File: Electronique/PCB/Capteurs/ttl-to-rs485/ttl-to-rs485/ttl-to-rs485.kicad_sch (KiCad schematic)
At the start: 4 parts, among them U1 HW-221, U2 JST-SH 4, U3 JST-SH4 motor, U4 TTL-RS485

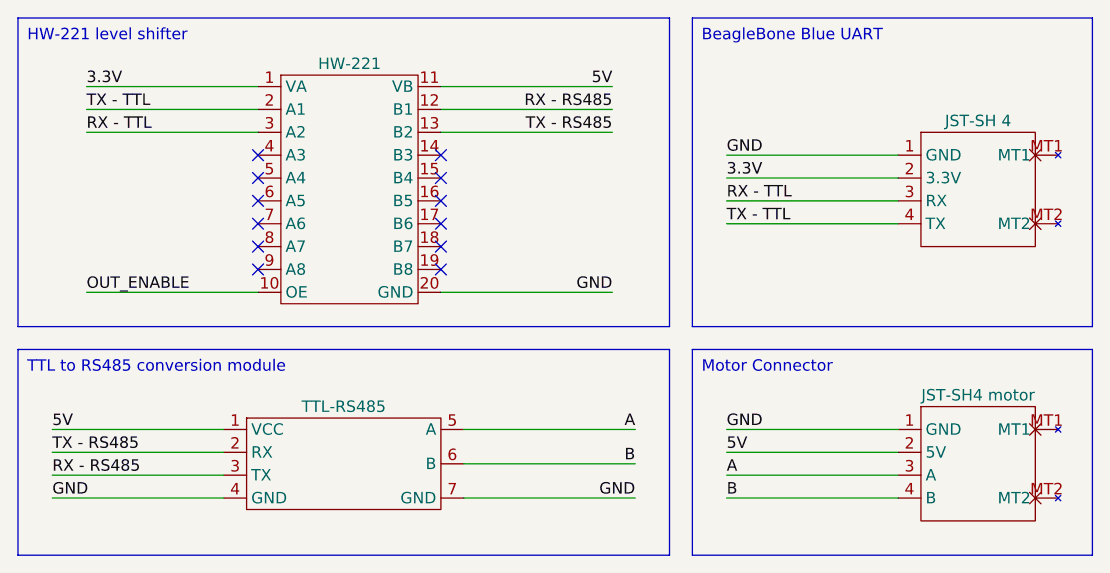
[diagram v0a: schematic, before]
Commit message: ttl to rs485 proto pcb
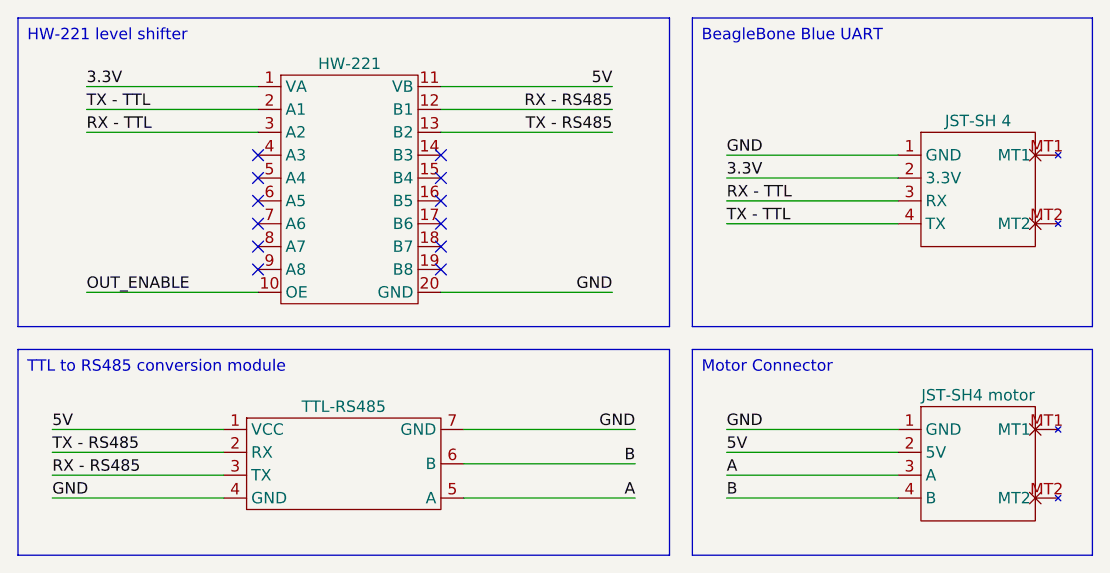
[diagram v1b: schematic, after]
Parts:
- U4: footprint Connector_PinHeader_2.54mm:PinHeader_1x04_P2.54mm_Vertical -> ttl-to-rs485:TTL-RS485
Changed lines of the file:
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@@
     (effects (font (size 1.27 1.27)) (justify left bottom))
   )
-  (label "GND" (at 153.67 119.38 180) (fields_autoplaced)
+  (label "GND" (at 153.67 111.76 180) (fields_autoplaced)
     (effects (font (size 1.27 1.27)) (justify right bottom))
   )
@@
     (effects (font (size 1.27 1.27)) (justify left bottom))
   )
-  (label "A" (at 153.67 111.76 180) (fields_autoplaced)
+  (label "A" (at 153.67 119.38 180) (fields_autoplaced)
     (effects (font (size 1.27 1.27)) (justify right bottom))
   )
@@
   (label "GND" (at 151.13 96.52 180) (fields_autoplaced)
     (effects (font (size 1.27 1.27)) (justify right bottom))
-  )
-  (symbol (lib_id "ttl-to-rs485:TTL-RS485") (at 121.92 115.57 0) (unit 1)
-    (in_bom yes) (on_board yes) (dnp no) (fields_autoplaced)
-    (property "Reference" "U4" (at 121.92 105.41 0)
-      (effects (font (size 1.27 1.27)) hide)
-    )
-    (property "Value" "TTL-RS485" (at 121.285 109.22 0)
-      (effects (font (size 1.27 1.27)))
-    )
-    (property "Footprint" "Connector_PinHeader_2.54mm:PinHeader_1x04_P2.54mm_Vertical" (at 121.92 123.19 0)
-      (effects (font (size 1.27 1.27)) hide)
-    )
-    (property "Datasheet" "" (at 109.22 115.57 0)
-      (effects (font (size 1.27 1.27)) hide)
-    )
-    (pin "1")
-    (pin "2")
-    (pin "3")
-    (pin "4")
-    (pin "5")
-    (pin "6")
-    (pin "7")
-    (instances
-      (project "ttl-to-rs485"
-        (path "/0267b611-6832-4bd8-91f6-9065e44bb5bf"
-          (reference "U4") (unit 1)
-        )
-      )
-    )
   )
   (symbol (lib_id "ttl-to-rs485:HW-221") (at 121.92 86.36 0) (unit 1)
@@
         )
       )
+    )
+  )
+  (symbol (lib_id "ttl-to-rs485:TTL-RS485") (at 121.92 115.57 0) (unit 1)
+    (in_bom yes) (on_board yes) (dnp no) (fields_autoplaced)
+    (property "Reference" "U4" (at 121.92 105.41 0)
+      (effects (font (size 1.27 1.27)) hide)
+    )
+    (property "Value" "TTL-RS485" (at 121.285 109.22 0)
+      (effects (font (size 1.27 1.27)))
+    )
+    (property "Footprint" "ttl-to-rs485:TTL-RS485" (at 121.92 123.19 0)
+      (effects (font (size 1.27 1.27)) hide)
+    )
+    (property "Datasheet" "" (at 109.22 115.57 0)
+      (effects (font (size 1.27 1.27)) hide)
+    )
+    (pin "1")
+    (pin "2")
+    (pin "3")
+    (pin "4")
+    (pin "5")
+    (pin "6")
+    (pin "7")
+    (instances
+      (project "ttl-to-rs485"
+        (path "/0267b611-6832-4bd8-91f6-9065e44bb5bf"
+          (reference "U4") (unit 1)
+        )
+      )

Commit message: update to ttl to rs485 pcb
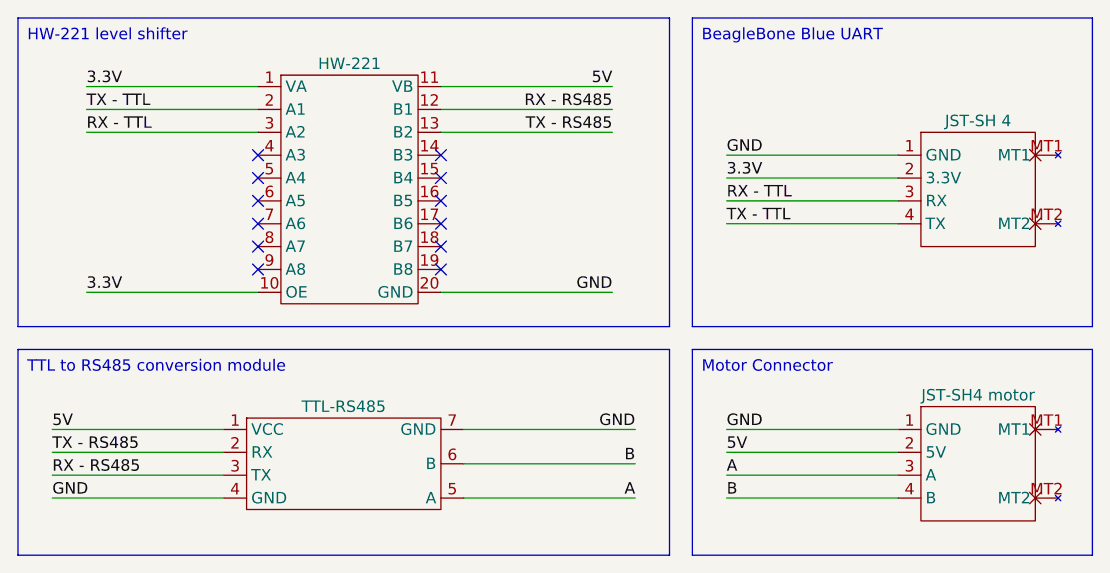
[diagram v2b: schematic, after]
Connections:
- net OUT_ENABLE is gone; now on net 3.3V: U1.10 (OE)
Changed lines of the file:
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@@
-    (effects (font (size 1.27 1.27)) (justify left bottom))
-  )
-  (label "OUT_ENABLE" (at 92.71 96.52 0) (fields_autoplaced)
     (effects (font (size 1.27 1.27)) (justify left bottom))
   )
@@
     (effects (font (size 1.27 1.27)) (justify left bottom))
   )
+  (label "3.3V" (at 92.71 96.52 0) (fields_autoplaced)
+    (effects (font (size 1.27 1.27)) (justify left bottom))
+  )
